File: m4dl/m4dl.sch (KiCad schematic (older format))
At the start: 88 parts, among them IC1 NCP380, IC2 STM32F405RxTx, IC3 MCP2562, J1 TEMP2-8, J2 PRESSURE, J3 WEST TOP, J4 EAST TOP, J7 USB, P1 SWD_TC, U1 MICROSD

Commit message: Update references to cusf-kicad
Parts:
- C10, C11, C12, C13, C17, C18, C3, C4: symbol main-rescue:C_Small -> Device:C_Small
- C14, C15, C16, C6, C7: symbol pressure-rescue:C_Small -> Device:C_Small
- C23, C24, C25, C26, C27, C29, C30, C31, C32, C33, C34, C35, C36: symbol temperature-rescue:C_Small -> Device:C_Small
- D2, D3, D4, D5: symbol pressure-rescue:ESD_DIODE -> agg-kicad:ESD_DIODE
- IC1: symbol pressure-rescue:NCP380 -> agg-kicad:NCP380
- IC2: symbol main-rescue:STM32F405RxTx -> agg-kicad:STM32F405RxTx
- IC?: symbol temperature-rescue:LTC2986 -> agg-kicad:LTC2986
- J1: symbol temperature-rescue:CONN_02x07 -> agg-kicad:CONN_02x07
- J2: symbol pressure-rescue:CONN_02x05 -> agg-kicad:CONN_02x05
- J7: symbol main-rescue:CONN_01x04 -> agg-kicad:CONN_01x04
- P1: symbol main-rescue:SWD_TC -> agg-kicad:SWD_TC
- R10, R11, R12, R8: symbol pressure-rescue:R -> Device:R
- R19, R20, R21, R22, R24, R25, R26, R27, R29, R30, R31, R32, R34, R35, R36: symbol temperature-rescue:R -> Device:R
- R2, R3, R4, R5, R6, R7: symbol main-rescue:R -> Device:R
- U1: symbol main-rescue:MICROSD-RESCUE-main -> agg-kicad:MICROSD

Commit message: Use cusf-kicad.lib instead of agg-kicad.lib
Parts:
- C19, C22, C? (x11): symbol agg-kicad:C -> cusf-kicad:C
- D10, D6, D7: symbol agg-kicad:LED -> cusf-kicad:LED
- D2, D3, D4, D5: symbol agg-kicad:ESD_DIODE -> cusf-kicad:ESD_DIODE
- IC1: symbol agg-kicad:NCP380 -> cusf-kicad:NCP380
- IC2: symbol agg-kicad:STM32F405RxTx -> cusf-kicad:STM32F405RxTx
- IC3: symbol agg-kicad:MCP2562 -> cusf-kicad:MCP2562
- IC?: symbol agg-kicad:LTC2986 -> cusf-kicad:LTC2986
- J1: symbol agg-kicad:CONN_02x07 -> cusf-kicad:CONN_02x07
- J2: symbol agg-kicad:CONN_02x05 -> cusf-kicad:CONN_02x05
- J3, J4: symbol agg-kicad:CONN_02x15 -> cusf-kicad:CONN_02x15
- J7: symbol agg-kicad:CONN_01x04 -> cusf-kicad:CONN_01x04
- P1: symbol agg-kicad:SWD_TC -> cusf-kicad:SWD_TC
- R13, R16, R17, R18, R?: symbol agg-kicad:R -> cusf-kicad:R
- U1: symbol agg-kicad:MICROSD -> cusf-kicad:MICROSD
- Y?: symbol agg-kicad:SMD_XTAL -> cusf-kicad:SMD_XTAL

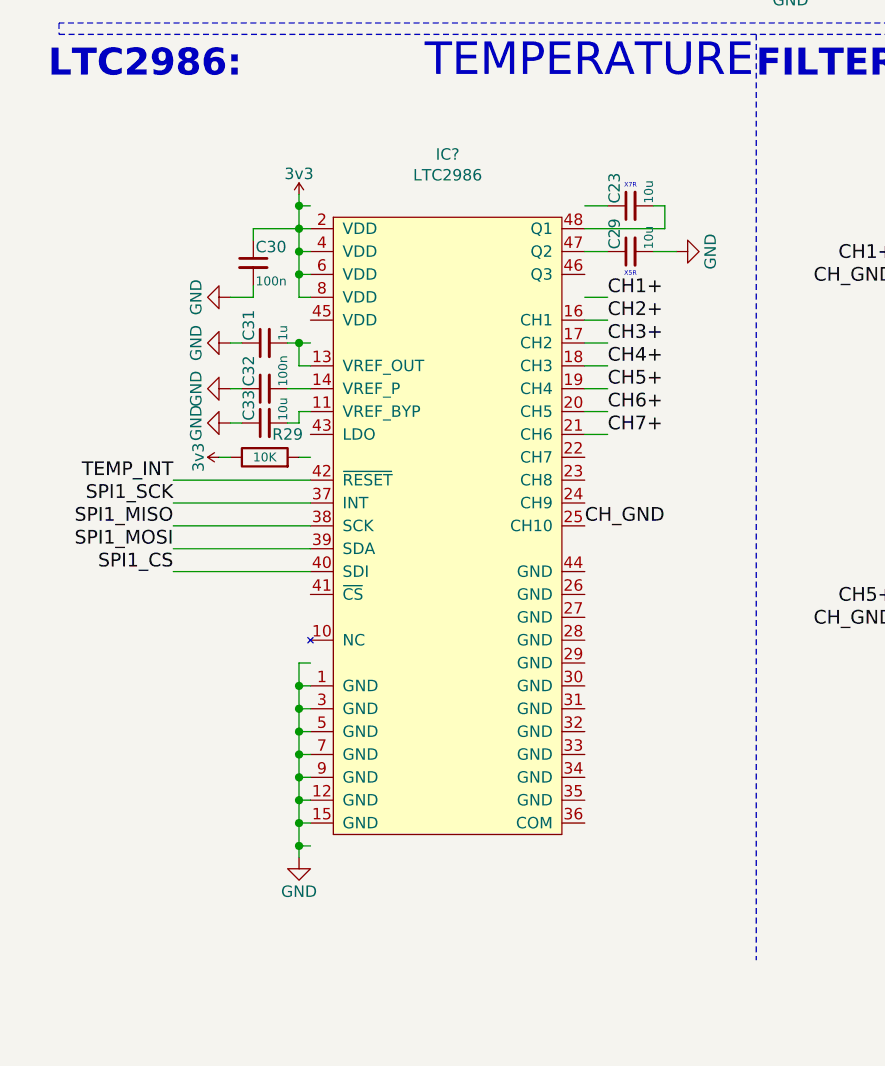
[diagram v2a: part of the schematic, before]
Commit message: Fix layout around LTC2986
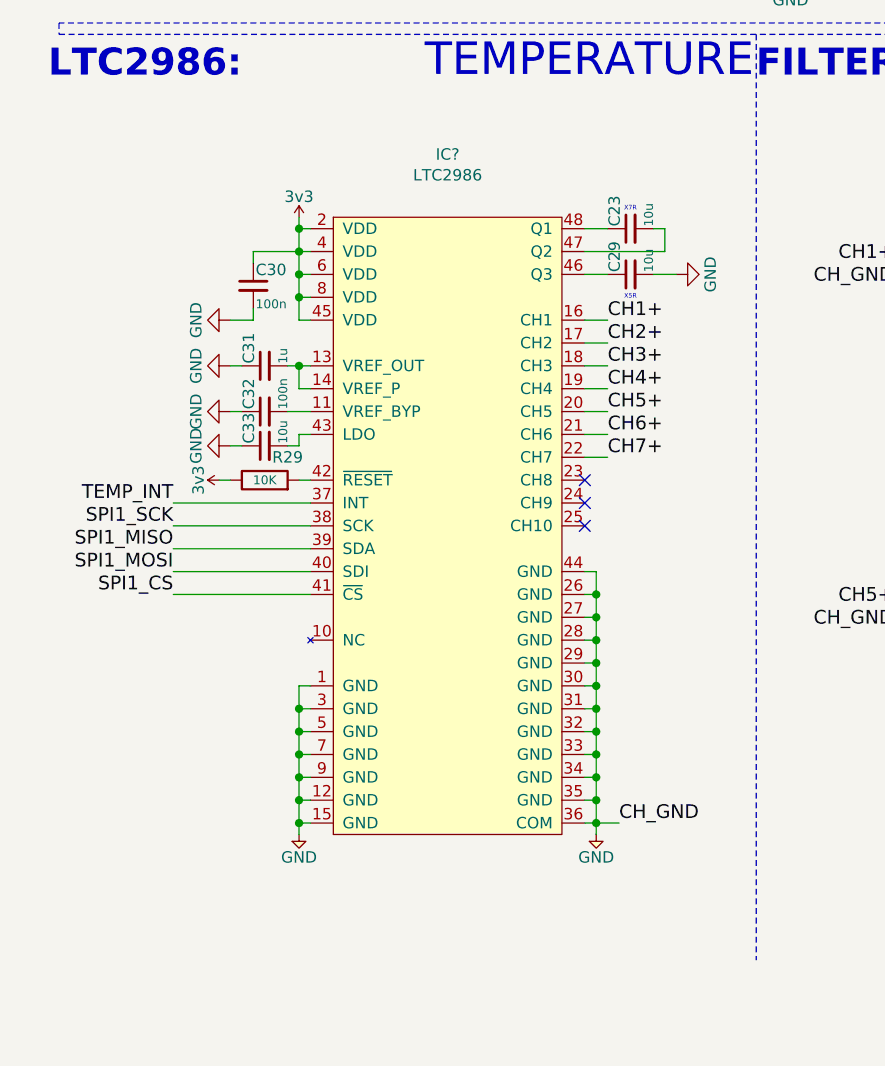
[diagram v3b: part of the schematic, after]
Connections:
- wire segments 528 -> 549
- no-connect marks 40 -> 43
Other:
- moved on the sheet: C23, C29, C30, C31, C32, C33, R29

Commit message: Merge sd into dl, convert symbols to cusf-kicad, and add UART
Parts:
- removed C10, C11, C12, C13, C3, C30, C32, C4: 100n, Capacitors_SMD:C_0603, symbol Device:C_Small
- removed C14, C15, C16, C24, C25, C26, C27, C34, C35, C36: 1n, Capacitors_SMD:C_0603, symbol Device:C_Small
- removed C17: 4u7, Capacitors_SMD:C_0603, symbol Device:C_Small
- removed C23: 10u, agg:0805, symbol Device:C_Small
- removed C31: 1u, Capacitors_SMD:C_0603, symbol Device:C_Small
- removed D4, D5: ESD_DIODE, agg:0402, symbol cusf-kicad:ESD_DIODE
- removed R10, R11, R12, R19, R20, R21, R22, R24, R25, R26, R27, R30, R31, R32, R34, R35, R36: 3.74K, Resistors_SMD:R_0603, symbol Device:R
- removed R2, R3, R4, R5, R6: 47K, Resistors_SMD:R_0603, symbol Device:R
- removed R29: 10K, Resistors_SMD:R_0603, symbol Device:R
- removed R7: 1k, agg:0603-L, symbol Device:R
- added C?: 100n, symbol cusf-kicad:C
- added C? (x10): 1n, symbol cusf-kicad:C
- added C? (x8): 100n, Capacitors_SMD:C_0603, symbol cusf-kicad:C
- added C?: 1u, Capacitors_SMD:C_0603, symbol cusf-kicad:C
- added C?: 4u7, Capacitors_SMD:C_0603, symbol cusf-kicad:C
- added C?: 10u, Capacitors_SMD:C_0603, symbol cusf-kicad:C
- added D? (x2): ESD_DIODE, agg:0402, symbol cusf-kicad:ESD_DIODE
- added IC?: ADuM1201, agg:SOIC-8, symbol cusf-kicad:ADuM1201
- added J?: UART, symbol Connector_Generic:Conn_01x04
- added R? (x5): 47k, symbol cusf-kicad:R
- added R?: 1k, symbol cusf-kicad:R
- added R? (x17): 3k74, symbol cusf-kicad:R
- added R?: 10k, symbol cusf-kicad:R
- C?: renamed from C18; symbol Device:C_Small -> cusf-kicad:C
- C?: renamed from C33; symbol Device:C_Small -> cusf-kicad:C
- C?: renamed from C29; symbol Device:C_Small -> cusf-kicad:C
- renumbered C6 to C?, C7 to C?, C19 to C?, C22 to C?, D3 to D?, D2 to D?, D6 to D?, D7 to D?, D10 to D?, IC2 to IC?, IC1 to IC?, IC3 to IC?, J2 to J?, J1 to J?, J7 to J?, J3 to J?, J4 to J?, P1 to P?, R8 to R?, R18 to R?, R13 to R?, R17 to R?, R16 to R?, U1 to U?
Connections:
- net 3v3: now also C?.1, C?.1, C?.1, C?.1, C?.1, C?.1, C?.1, C?.1, C?.2, IC?.1 (VDD1), IC?.8 (VDD2), J?.4 (Pin_4), R?.1, R?.1, R?.1, R?.1, R?.1, R?.1; no longer J?.7
- net CH1+: now also C?.1, R?.1
- net CH2+: now also C?.1, R?.1
- net CH3+: now also C?.1, R?.1
- net CH4+: now also C?.1, R?.1
- net CH5+: now also C?.1, R?.1
- net CH6+: now also C?.1, R?.1
- net CH7+: now also C?.1, R?.1
- net GND: now also C?.1, C?.1, C?.1, C?.2, C?.2, C?.2, C?.2, C?.2, C?.2, C?.2, C?.2, C?.2, C?.2, C?.2, C?.2, C?.2, C?.2, C?.2, C?.2, C?.2, C?.2, D?.1, D?.1, IC?.4 (GND1), IC?.5 (GND2), J?.3 (Pin_3), R?.1, R?.1, R?.1, R?.1, R?.1, R?.1, R?.1
- net OTG_HS_VBUS: now also R?.2
- net P1+: now also R?.2
- net P2+: now also D?.2, R?.2
- net P3+: now also D?.2, R?.2
- net PRESSURE1: now also C?.1, IC?.7 (IN_A), R?.1
- net PRESSURE2: now also C?.1, IC?.6 (OUT_B), R?.1
- net PRESSURE3: now also C?.1, R?.1
- net SDIO_CMD: now also R?.2
- net SDIO_D0: now also R?.2
- net SDIO_D1: now also R?.2
- net SDIO_D2: now also R?.2
- net SDIO_D3: now also R?.2
- net TEMP1+: now also R?.2
- net TEMP1-: now also R?.2
- net TEMP2+: now also R?.2
- net TEMP2-: now also R?.2
- net TEMP3+: now also R?.2
- net TEMP3-: now also R?.2
- net TEMP4+: now also R?.2
- net TEMP4-: now also R?.2
- net TEMP5+: now also R?.2
- net TEMP5-: now also R?.2
- net TEMP6+: now also R?.2
- net TEMP6-: now also R?.2
- net TEMP7+: now also R?.2
- net TEMP7-: now also R?.2
- net UART_RX: now also IC?.3 (IN_B), J?.2 (Pin_2)
- net UART_TX: now also IC?.2 (OUT_A), J?.1 (Pin_1)
- net at IC?.13 (VREF_OUT), IC?.14 (VREF_P): now also C?.2
- net at IC?.11 (VREF_BYP): now also C?.2
- net at IC?.42 (~RESET): now also R?.2
- net at IC?.48 (Q1): now also C?.1
- net at IC?.47 (Q2): now also C?.2
- net at J?.1: now also R?.1
- new net 3v3_DL: J?.7
- no-connect marks 43 -> 54
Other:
- note added: "PA2(TX) <-> Pressure 1\nPA3 (RX) <-> Pressure 2"
- note removed: "Connection to pressure wires"
- note removed: "Connection to temperature wires\nsplit up to fit on board"
- note removed: "External"
- note removed: "Internal"
- note removed: "Working Voltage"
- note removed: "X5R"
- note removed: "X7R"
- moved on the sheet: C?, J?

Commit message: Correct symbols
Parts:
- removed R?: 110k, agg:0402-L, symbol Device:R
- added R?: 110k, symbol cusf-kicad:R
- C? (x2): symbol Device:C_Small -> cusf-kicad:C
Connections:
- net 3v3: now also C?.2; no longer C?.1
- net GND: now also C?.1, R?.2; no longer C?.2
- net at IC?.2 (ILIM): now also R?.1
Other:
- moved on the sheet: C?, D?
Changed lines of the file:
@@
 	1    0    0    -1
 $EndComp
-$Comp
-L power:GND #PWR?
-U 1 1 5760A05E
-P 15500 4750
-F 0 "#PWR?" H 15500 4500 50  0001 C CNN
-F 1 "GND" H 15500 4600 50  0000 C CNN
-F 2 "" H 15500 4750 50  0000 C CNN
-F 3 "" H 15500 4750 50  0000 C CNN
-	1    15500 4750
-	1    0    0    -1
-$EndComp
-Wire Wire Line
-	15500 4500 15500 4750
-Wire Wire Line
-	15500 4300 15500 4000
+Wire Wire Line
+	15500 4450 15500 4750
+Wire Wire Line
+	15500 4250 15500 4000
 $Comp
 L cusf-kicad:ESD_DIODE D?
 U 1 1 57609B08
-P 15500 4400
-F 0 "D?" H 15450 4500 50  0000 L CNN
-F 1 "ESD_DIODE" H 15450 4300 50  0001 L CNN
-F 2 "agg:0402" H 15450 4200 50  0001 L CNN
-F 3 "" H 15400 4400 50  0001 C CNN
-F 4 "2368169" H 15450 4100 50  0001 L CNN "Farnell"
-	1    15500 4400
+P 15500 4350
+F 0 "D?" H 15450 4450 50  0000 L CNN
+F 1 "ESD_DIODE" H 15450 4250 50  0001 L CNN
+F 2 "agg:0402" H 15450 4150 50  0001 L CNN
+F 3 "" H 15400 4350 50  0001 C CNN
+F 4 "2368169" H 15450 4050 50  0001 L CNN "Farnell"
+	1    15500 4350
 	0    -1   -1   0
 $EndComp
@@
 Text Notes 14100 3550 2    118  ~ 24
 CURRENT LIMITING:
-$Comp
-L power:GND #PWR?
-U 1 1 57608A21
-P 13350 4750
-F 0 "#PWR?" H 13350 4500 50  0001 C CNN
-F 1 "GND" H 13350 4600 50  0000 C CNN
-F 2 "" H 13350 4750 50  0000 C CNN
-F 3 "" H 13350 4750 50  0000 C CNN
-	1    13350 4750
-	1    0    0    -1
-$EndComp
-Wire Wire Line
-	13350 4500 13350 4750
-Wire Wire Line
-	13350 4300 13350 4050
-$Comp
-L power:GND #PWR?
-U 1 1 57608A18
-P 13600 4750
-F 0 "#PWR?" H 13600 4500 50  0001 C CNN
-F 1 "GND" H 13600 4600 50  0000 C CNN
-F 2 "" H 13600 4750 50  0000 C CNN
-F 3 "" H 13600 4750 50  0000 C CNN
-	1    13600 4750
-	1    0    0    -1
-$EndComp
 Connection ~ 13600 4050
 Wire Wire Line
@@
 NoConn ~ 13900 4350
 Wire Wire Line
-	14800 4650 14800 4750
-Wire Wire Line
-	14800 4250 14800 4350
-Wire Wire Line
 	14700 4250 14800 4250
-Wire Wire Line
-	15100 4500 15100 4750
-Wire Wire Line
-	15100 4300 15100 4000
-$Comp
-L power:GND #PWR?
-U 1 1 57608A04
-P 15100 4750
-F 0 "#PWR?" H 15100 4500 50  0001 C CNN
-F 1 "GND" H 15100 4600 50  0000 C CNN
-F 2 "" H 15100 4750 50  0000 C CNN
-F 3 "" H 15100 4750 50  0000 C CNN
-	1    15100 4750
-	1    0    0    -1
-$EndComp
 $Comp
 L cusf-kicad:3v3 #PWR?
@@
 F 3 "" H 15100 4000 60  0000 C CNN
 	1    15100 4000
-	1    0    0    -1
-$EndComp
-$Comp
-L power:GND #PWR?
-U 1 1 576089F8
-P 14800 4750
-F 0 "#PWR?" H 14800 4500 50  0001 C CNN
-F 1 "GND" H 14800 4600 50  0000 C CNN
-F 2 "" H 14800 4750 50  0000 C CNN
-F 3 "" H 14800 4750 50  0000 C CNN
-	1    14800 4750
 	1    0    0    -1
 $EndComp
@@
 $EndComp
 $Comp
-L power:GND #PWR?
-U 1 1 576089E6
-P 13850 4750
-F 0 "#PWR?" H 13850 4500 50  0001 C CNN
-F 1 "GND" H 13850 4600 50  0000 C CNN
-F 2 "" H 13850 4750 50  0000 C CNN
-F 3 "" H 13850 4750 50  0000 C CNN
-	1    13850 4750
-	1    0    0    -1
-$EndComp
-$Comp
-L Device:R R?
-U 1 1 576089D6
-P 14800 4500
-F 0 "R?" V 14700 4500 50  0000 C CNN
-F 1 "110k" V 14800 4500 39  0000 C CNN
-F 2 "agg:0402-L" V 14730 4500 50  0001 C CNN
-F 3 "" H 14800 4500 50  0000 C CNN
-F 4 "2502502" V 14800 4500 60  0001 C CNN "Farnell"
-	1    14800 4500
-	-1   0    0    -1
-$EndComp
-$Comp
-L Device:C_Small C?
+L cusf-kicad:C C?
 U 1 1 576089C8
-P 15100 4400
-F 0 "C?" H 15110 4470 50  0000 L CNN
-F 1 "1u" H 15110 4320 50  0000 L CNN
-F 2 "agg:0402-L" H 15100 4400 50  0001 C CNN
-F 3 "" H 15100 4400 50  0000 C CNN
-F 4 "2346884" H 15100 4400 60  0001 C CNN "Farnell"
-	1    15100 4400
-	1    0    0    -1
-$EndComp
-$Comp
-L Device:C_Small C?
+P 15100 4300
+F 0 "C?" H 15110 4370 50  0000 L CNN
+F 1 "1u" H 15110 4220 50  0000 L CNN
+F 2 "agg:0402-L" H 15100 4300 50  0001 C CNN
+F 3 "" H 15100 4300 50  0000 C CNN
+F 4 "2346884" H 15100 4300 60  0001 C CNN "Farnell"
+	1    15100 4300
+	0    1    1    0
+$EndComp
+$Comp
+L cusf-kicad:C C?
 U 1 1 576089C1
-P 13350 4400
-F 0 "C?" H 13360 4470 50  0000 L CNN
-F 1 "1u" H 13360 4320 50  0000 L CNN
-F 2 "agg:0402-L" H 13350 4400 50  0001 C CNN
-F 3 "" H 13350 4400 50  0000 C CNN
-F 4 "2346884" H 13350 4400 60  0001 C CNN "Farnell"
-	1    13350 4400
-	-1   0    0    -1
+P 13350 4450
+F 0 "C?" V 13450 4450 50  0000 L CNN
+F 1 "1u" V 13350 4450 50  0000 L CNN
+F 2 "agg:0402-L" H 13350 4450 50  0001 C CNN
+F 3 "" H 13350 4450 50  0000 C CNN
+F 4 "2346884" H 13350 4450 60  0001 C CNN "Farnell"
+	1    13350 4450
+	0    1    -1   0
 $EndComp
 $Comp
@@
 	0    -1   -1   0
 $EndComp
+Wire Wire Line
+	13350 4050 13350 4350
+Wire Wire Line
+	13350 4450 13350 4750
+$Comp
+L cusf-kicad:GND #PWR?
+U 1 1 6277D207
+P 15500 4750
+F 0 "#PWR?" H 15370 4790 50  0001 L CNN
+F 1 "GND" H 15500 4650 50  0000 C CNN
+F 2 "" H 15500 4750 50  0001 C CNN
+F 3 "" H 15500 4750 50  0001 C CNN
+	1    15500 4750
+	1    0    0    -1
+$EndComp
+$Comp
+L cusf-kicad:GND #PWR?
+U 1 1 6277E451
+P 15100 4750
+F 0 "#PWR?" H 14970 4790 50  0001 L CNN
+F 1 "GND" H 15100 4650 50  0000 C CNN
+F 2 "" H 15100 4750 50  0001 C CNN
+F 3 "" H 15100 4750 50  0001 C CNN
+	1    15100 4750
+	1    0    0    -1
+$EndComp
+$Comp
+L cusf-kicad:GND #PWR?
+U 1 1 6277E747
+P 14800 4750
+F 0 "#PWR?" H 14670 4790 50  0001 L CNN
+F 1 "GND" H 14800 4650 50  0000 C CNN
+F 2 "" H 14800 4750 50  0001 C CNN
+F 3 "" H 14800 4750 50  0001 C CNN
+	1    14800 4750
+	1    0    0    -1
+$EndComp
+$Comp
+L cusf-kicad:GND #PWR?
+U 1 1 6277E96B
+P 13850 4750
+F 0 "#PWR?" H 13720 4790 50  0001 L CNN
+F 1 "GND" H 13850 4650 50  0000 C CNN
+F 2 "" H 13850 4750 50  0001 C CNN
+F 3 "" H 13850 4750 50  0001 C CNN
+	1    13850 4750
+	1    0    0    -1
+$EndComp
+$Comp
+L cusf-kicad:GND #PWR?
+U 1 1 6277EB37
+P 13600 4750
+F 0 "#PWR?" H 13470 4790 50  0001 L CNN
+F 1 "GND" H 13600 4650 50  0000 C CNN
+F 2 "" H 13600 4750 50  0001 C CNN
+F 3 "" H 13600 4750 50  0001 C CNN
+	1    13600 4750
+	1    0    0    -1
+$EndComp
+$Comp
+L cusf-kicad:GND #PWR?
+U 1 1 6277ECDE
+P 13350 4750
+F 0 "#PWR?" H 13220 4790 50  0001 L CNN
+F 1 "GND" H 13350 4650 50  0000 C CNN
+F 2 "" H 13350 4750 50  0001 C CNN
+F 3 "" H 13350 4750 50  0001 C CNN
+	1    13350 4750
+	1    0    0    -1
+$EndComp
+$Comp
+L cusf-kicad:R R?
+U 1 1 62780D72
+P 14800 4450
+F 0 "R?" H 14850 4400 50  0000 C CNN
+F 1 "110k" H 14850 4500 50  0000 C CNN
+F 2 "" H 14800 4450 50  0001 C CNN
+F 3 "" H 14800 4450 50  0001 C CNN
+	1    14800 4450
+	0    1    1    0
+$EndComp
+Wire Wire Line
+	14800 4250 14800 4450
+Wire Wire Line
+	14800 4550 14800 4750
+Wire Wire Line
+	15100 4000 15100 4300
+Wire Wire Line
+	15100 4400 15100 4750
 $EndSCHEMATC
